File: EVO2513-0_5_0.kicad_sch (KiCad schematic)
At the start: 0 parts

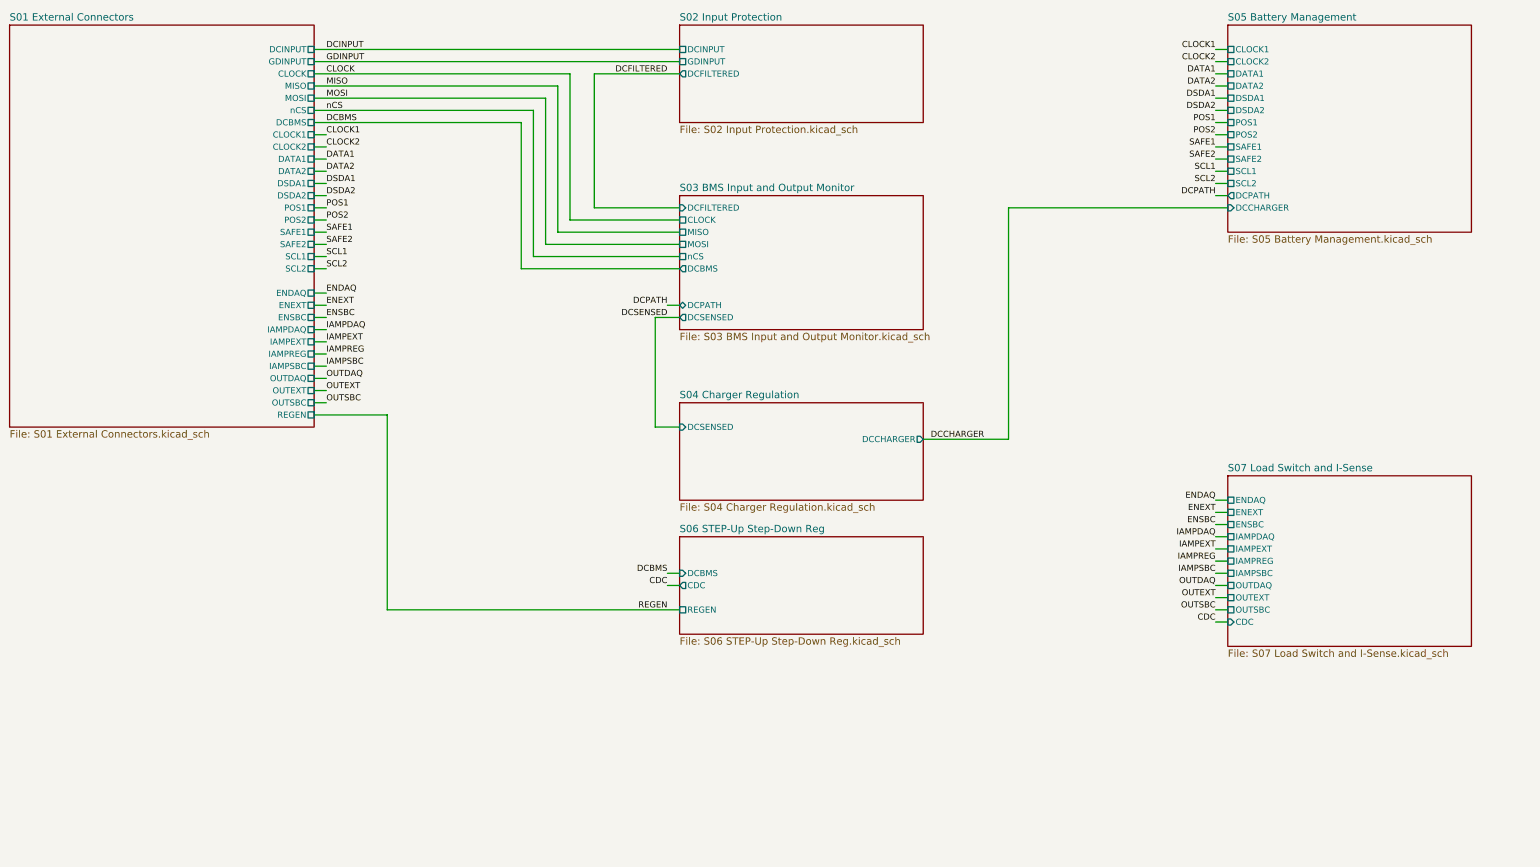
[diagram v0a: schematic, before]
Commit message: Add a PCAL9714 SPI I/O expander for the load-switch enables and faults
New sheet S08 with U11 (PCAL9714, HVQFN-24) on the shared CLOCK/MOSI/MISO
bus. J3.32, which was ENSBC, becomes its chip select nCSIO.

- P0_0-P0_2 drive ENDAQ, ENSBC and ENEXT. J3.34/J3.36 become MCU_ENDAQ
  and MCU_ENEXT, and each reaches its enable only through a DNP 0R link
  (R96-R98). R95 links nCSIO to the expander CS.
- P0_4-P0_6 read the U6/U7/U9 power-good signals, and P0_7 reads U5
  nFLT/nINT.
- REGEN stays a direct J3.12 signal.
- RESET is divided from +12V (R99 100K, R100 40.2K), so the expander
  stays in reset while the 12 V rail is off.
- Pull-ups on CS and INT (R93, R94) and decoupling (C58, C59).

The README gains the port map, the links and the board work. The board
still needs Update PCB from Schematic.

Co-Authored-By: Claude Opus 5.5 <noreply@anthropic.com>
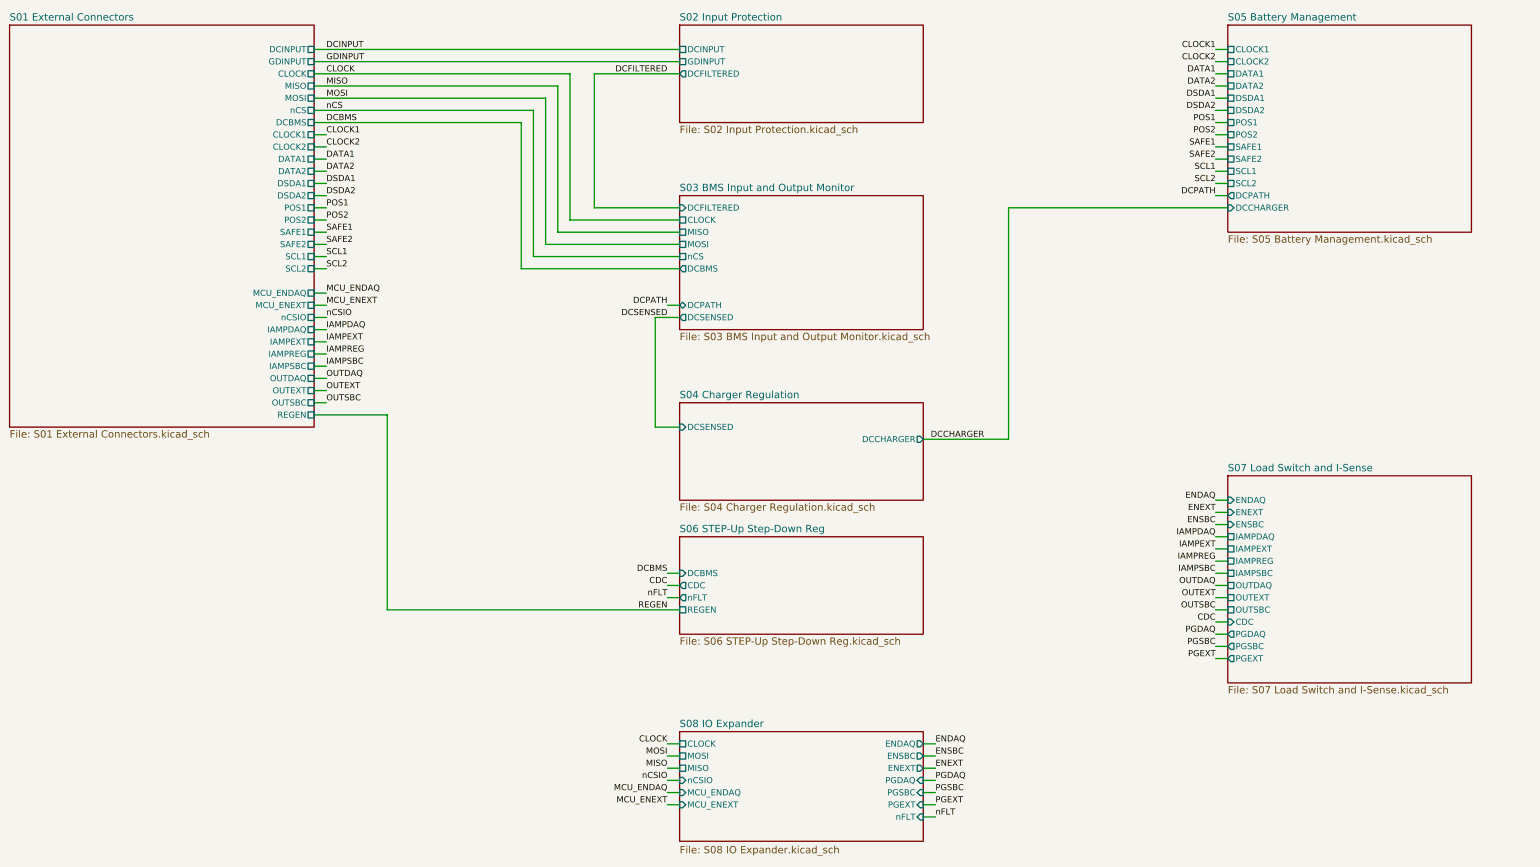
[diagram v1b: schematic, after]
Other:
- added sheet S08 IO Expander (S08 IO Expander.kicad_sch)
- sheet S01 External Connectors ports: added MCU_ENDAQ, MCU_ENEXT, nCSIO; removed ENDAQ, ENEXT, ENSBC
- sheet S06 STEP-Up Step-Down Reg ports: added nFLT; removed none
- sheet S07 Load Switch and I-Sense ports: added PGDAQ, PGEXT, PGSBC; removed none

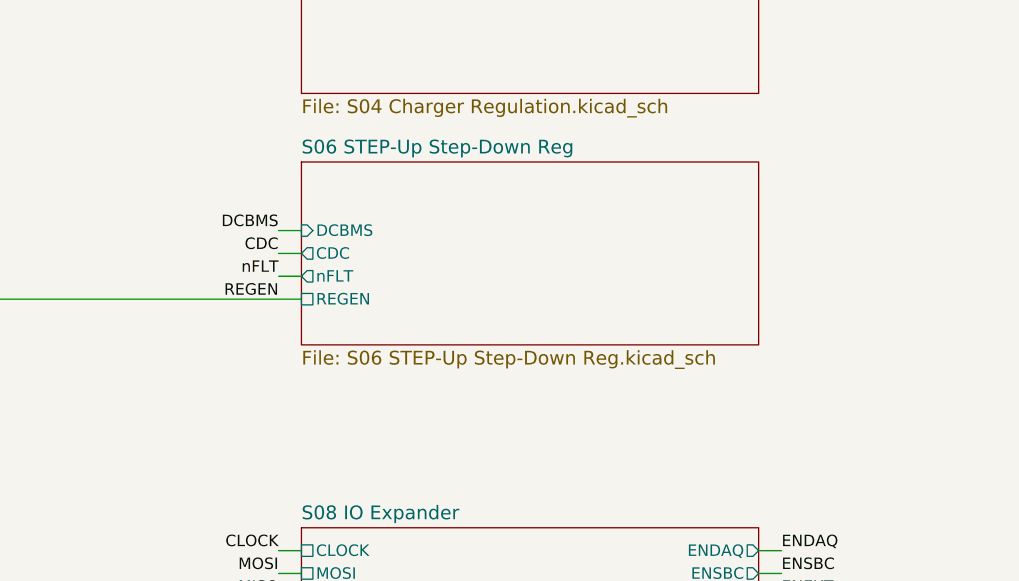
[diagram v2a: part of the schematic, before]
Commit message: BOM consolidation, OVLO divider to 1%, U5 fixes and I2C config option
- Consolidate passives: 1uF 50V to 0603, 100nF to 50V X7R 0402,
  10uF to 50V X7R 1210, 220nF to 0603, 10R to 0402 (100 -> 90 BOM lines)
- TPS22811 OVLO divider 1M/102K 0.1% -> 1M/100K 1% (12.6V min trip)
- U5 LM51772: C30 -> R102 10K to GND (VCC1 disabled), C32 -> 22uF 16V 0805,
  R29 1.9K -> 1.87K to sit inside the CFG4 window
- Add DNP I2C configuration option for U5 (R103-R107) on J3.34/J3.36,
  shared with R97/R98 fallback
- Document all changes in README.md

Co-Authored-By: Claude Opus 5.5 <noreply@anthropic.com>
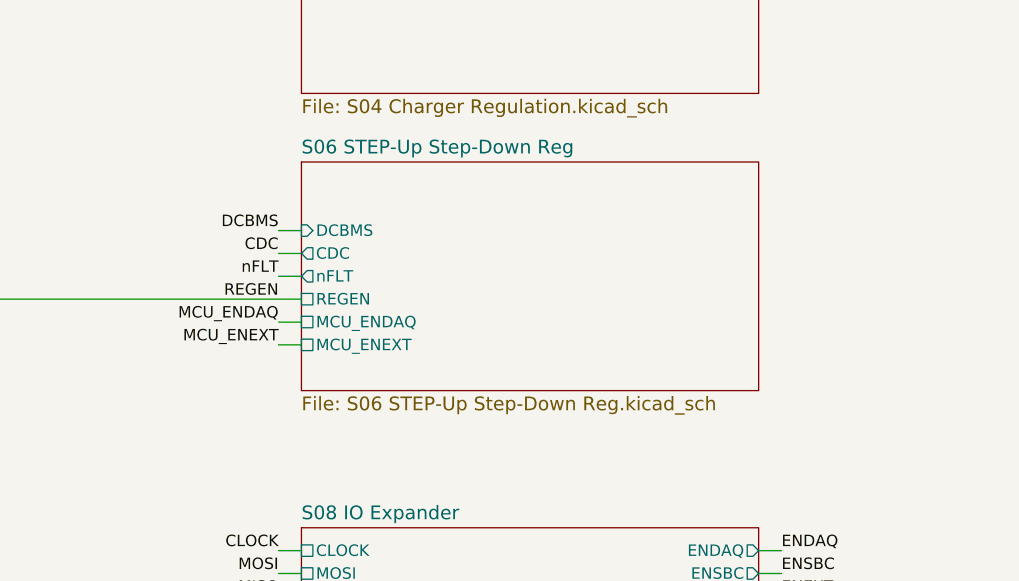
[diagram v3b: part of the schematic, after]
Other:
- sheet S06 STEP-Up Step-Down Reg ports: added MCU_ENDAQ, MCU_ENEXT; removed none
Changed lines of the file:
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@@
+		)
+	)
+	(wire
+		(pts
+			(xy 187.96 162.56) (xy 190.5 162.56)
+		)
+		(stroke
+			(width 0)
+			(type default)
+		)
+	)
+	(label "MCU_ENDAQ"
+		(at 187.96 162.56 180)
+		(effects
+			(font
+				(size 1.27 1.27)
+			)
+			(justify right bottom)
+		)
+	)
+	(wire
+		(pts
+			(xy 187.96 165.1) (xy 190.5 165.1)
+		)
+		(stroke
+			(width 0)
+			(type default)
+		)
+	)
+	(label "MCU_ENEXT"
+		(at 187.96 165.1 180)
+		(effects
+			(font
+				(size 1.27 1.27)
+			)
+			(justify right bottom)
 		)
 	)
@@
 	(sheet
 		(at 190.5 144.78)
-		(size 50.8 20.32)
+		(size 50.8 25.4)
 		(exclude_from_sim no)
 		(in_bom yes)
@@
 		)
 		(property "Sheetfile" "S06 STEP-Up Step-Down Reg.kicad_sch"
-			(at 190.5 165.687 0)
+			(at 190.5 170.767 0)
 			(show_name no)
 			(do_not_autoplace no)
@@
 			(effects
 				(font
+					(size 1.27 1.27)
+				)
+				(justify left)
+			)
+		)
+		(pin "MCU_ENDAQ" passive
+			(at 190.5 162.56 180)
+			(effects
+				(font
+					(size 1.27 1.27)
+				)
+				(justify left)
+			)
+		)
+		(pin "MCU_ENEXT" passive
+			(at 190.5 165.1 180)
+			(effects
+				(font

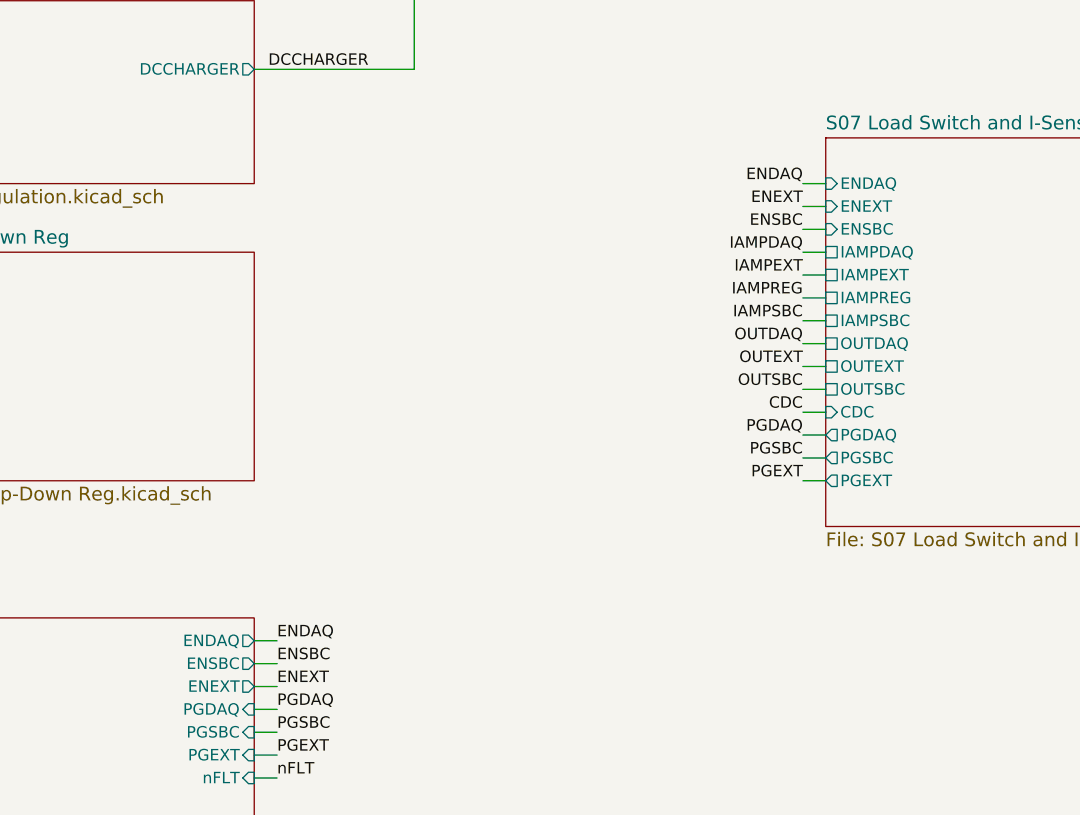
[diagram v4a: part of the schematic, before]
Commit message: Add an 11 V undervoltage lockout to the DAQ load switch
- R108 100K from +12V over R49 (100K -> 12K) on U6 EN/UVLO: on at 11.2 V
  (10.77-11.69 V), off at 10.17 V (9.83-10.66 V). The TPS22811's fixed
  hysteresis makes 11 V the turn-on point.
- Q24 (BSS138) from EN/UVLO to GND takes over the enable. Its gate is biased
  from +12V by R109 100K / R110 27K (2.55 V), so U6 stays in shutdown when
  the expander is in reset, unpowered, or the MCU board is off.
- The expander net ENDAQ is now nENDAQ, active low (S07, S08, root sheet).
  The gate stays under 3.3 V, so P0_0 can stay push-pull and the R97
  fallback can drive it from a 3.3 V MCU pin.
- S07 note marks the DAQ circuit as deliberate; S08 notes and README
  updated.

The PCB still needs Update PCB from Schematic: Q24 and R108-R110 are
missing, R49 has its old value, and /ENDAQ is split into two nets.

Co-Authored-By: Claude Opus 5.5 <noreply@anthropic.com>
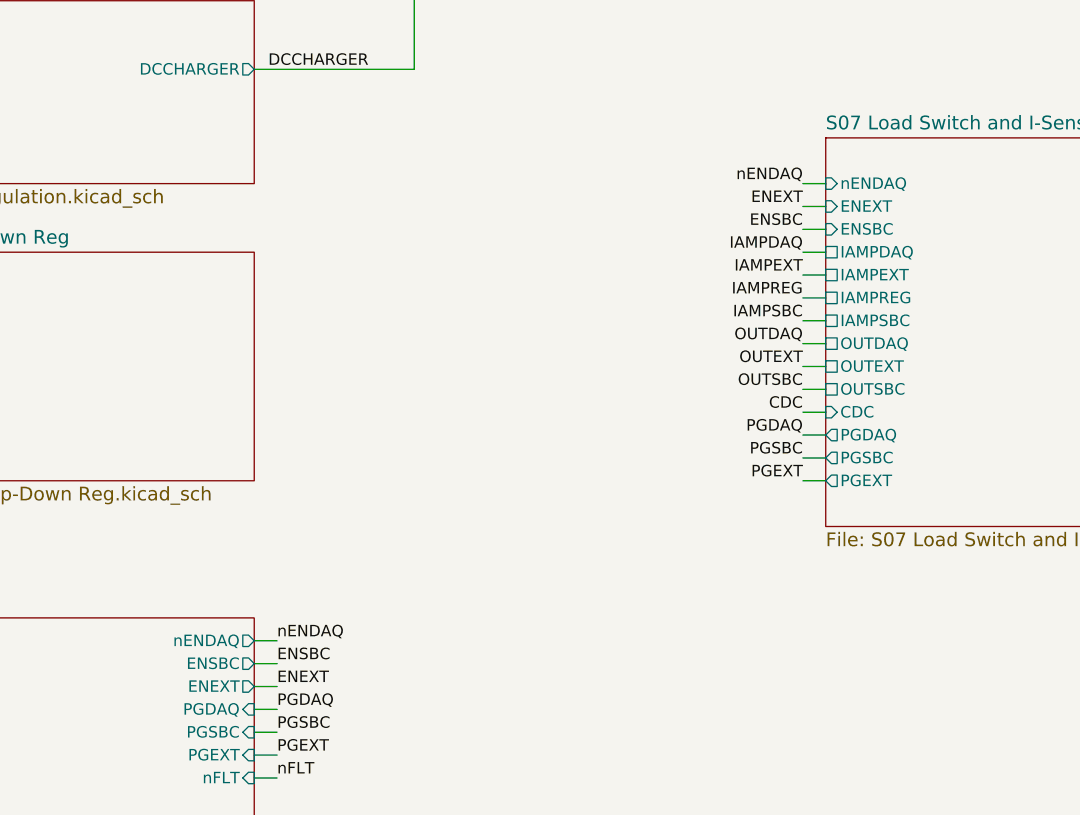
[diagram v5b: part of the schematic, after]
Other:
- sheet S07 Load Switch and I-Sense ports: added nENDAQ; removed ENDAQ
- sheet S08 IO Expander ports: added nENDAQ; removed ENDAQ
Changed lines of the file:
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@@
 		)
 	)
-	(label "ENDAQ"
+	(label "nENDAQ"
 		(at 243.84 187.96 0)
 		(effects
@@
 		)
 	)
-	(label "ENDAQ"
+	(label "nENDAQ"
 		(at 302.26 137.16 180)
 		(effects
@@
 			)
 		)
-		(pin "ENDAQ" input
+		(pin "nENDAQ" input
 			(at 304.8 137.16 180)
 			(effects
@@
 			)
 		)
-		(pin "ENDAQ" output
+		(pin "nENDAQ" output
 			(at 241.3 187.96 0)
 			(effects

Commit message: Revision 0.6.0 on the sheets, title and docs
- SCH_REVISION and SCH_VERSION W16 -> 0.6.0, so each sheet's REVISION
  field matches BOARD_NUMBER EVO2513-0.6.0 on the silkscreen.
- Root sheet title EVO2513 v0.6.0.
- README and FIRMWARE_NOTES headings to v0.6.0. The README says 0.6.0
  is the 0.5.0 field-test design with the W16 review changes, and that
  the files keep their 0_5_0 names.
- FIRMWARE_NOTES no longer calls this revision final.

Co-Authored-By: Claude Opus 5.5 <noreply@anthropic.com>
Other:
- title: EvoOne BMS (EVO2513 v0.5.0) -> EvoOne BMS (EVO2513 v0.6.0)
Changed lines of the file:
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@@
 	(paper "A3")
 	(title_block
-		(title "EvoOne BMS (EVO2513 v0.5.0)")
+		(title "EvoOne BMS (EVO2513 v0.6.0)")
 		(rev "${SCH_REVISION}")
 		(company "${COMP_NAME}")
